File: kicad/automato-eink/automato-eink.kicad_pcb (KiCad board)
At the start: 2 copper layers, 20 parts, among them J1 Conn_01x24, J2 Conn_01x08_Male, Q1 Q_NMOS_GDS

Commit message: first route
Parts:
- added L1: 68uH, Inductor_SMD:L_7.3x7.3_H3.5, F.Cu at (169.0, 107.0)
- moved C11 47.3 mm to (186.3, 95.0)
- moved C3 43.1 mm to (186.2, 108.5)
- moved J1 41.5 mm to (193.8, 107.8), turned to 90 degrees
- moved C12 41.0 mm to (186.3, 92.8)
- moved C6 40.3 mm to (186.2, 101.8)
- moved C9 38.3 mm to (186.3, 110.8)
- moved C4 36.7 mm to (186.2, 106.2)
- moved D1 35.0 mm to (178.0, 101.8)
- moved D3 32.7 mm to (178.0, 107.8), turned to 180 degrees
- moved C5 31.2 mm to (186.3, 104.0)
- moved C10 29.5 mm to (186.3, 97.2)
- moved D2 27.7 mm to (177.9, 104.8), turned to 180 degrees
- moved C7 23.3 mm to (186.2, 113.0)
- moved C8 17.9 mm to (186.2, 99.5)
- moved J2 14.4 mm to (140.2, 117.8), turned to 180 degrees
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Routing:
- net /RST: track 0.00 -> 81.8 mm, vias 0 -> 2
- net /DC: track 0.00 -> 80.8 mm, vias 0 -> 2
- net /CS: track 0.00 -> 80.0 mm, vias 0 -> 2
- net /SCLK: track 0.00 -> 79.0 mm, vias 0 -> 2
- net /BUSY: track 0.00 -> 78.6 mm
- net /SDI: track 0.00 -> 77.9 mm, vias 0 -> 2
- net GND: track 0.00 -> 35.1 mm, vias 0 -> 9
- net /RESE: track 0.00 -> 24.9 mm, vias 0 -> 2
- net /PREVGL: track 0.00 -> 24.5 mm, vias 0 -> 2
- net /PREVGH: track 0.00 -> 22.6 mm, vias 0 -> 2
- net /GDR: track 0.00 -> 18.7 mm, vias 0 -> 2
- net +3V3: track 0.00 -> 15.0 mm, vias 0 -> 2
- net Net-(C12-Pad2): track 0.00 -> 11.6 mm
- net Net-(C10-Pad2): track 0.00 -> 8.26 mm
- net Net-(C2-Pad2): track 0.00 -> 6.69 mm
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- added copper zone on F.Cu, net +3V3
- added copper zone on B.Cu, net GND
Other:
- board outline added: 62.5 x 35 mm
- net class Default: clearance 0.2 -> 0.1524; trace_width 0.25 -> 0.2
- rule trace_clearance: 0.2 -> 0.1524
- board text added: "AUTOMATO EInk rev 1"

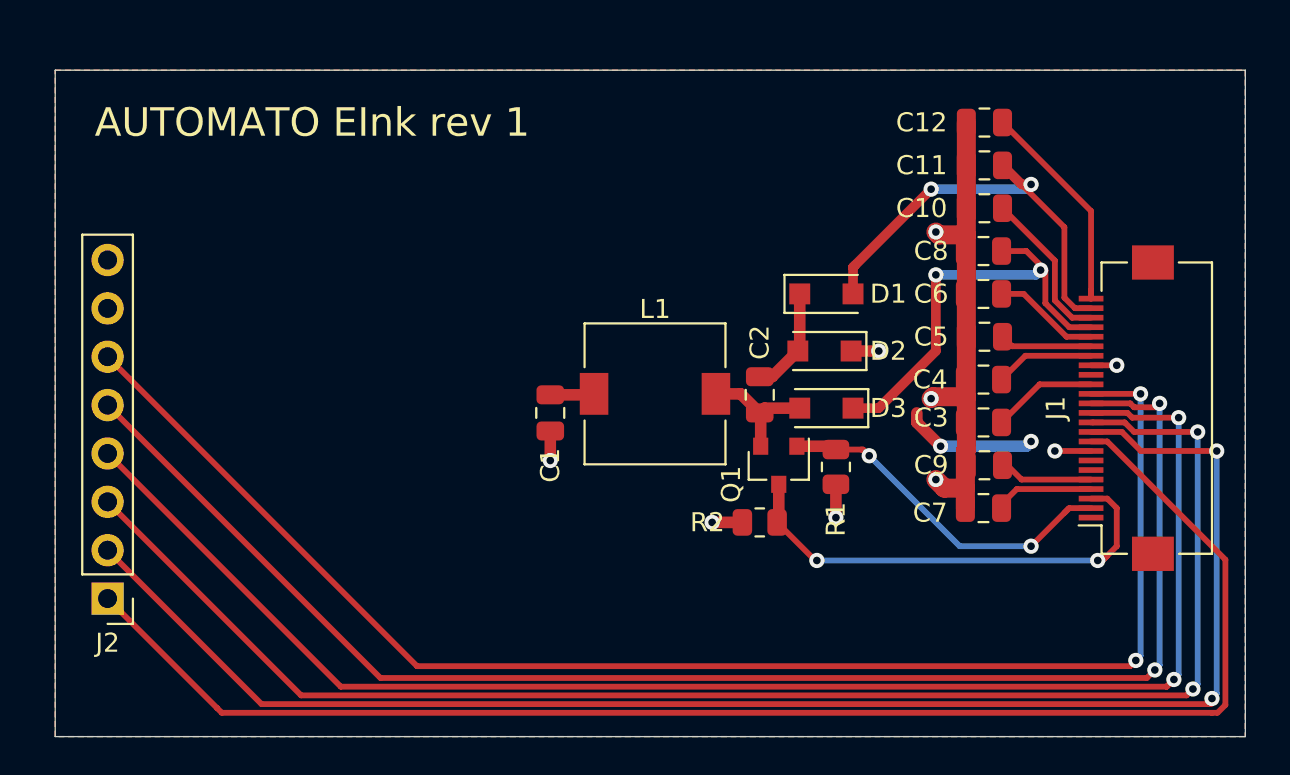
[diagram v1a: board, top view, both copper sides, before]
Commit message: update inductor, add stand-offs
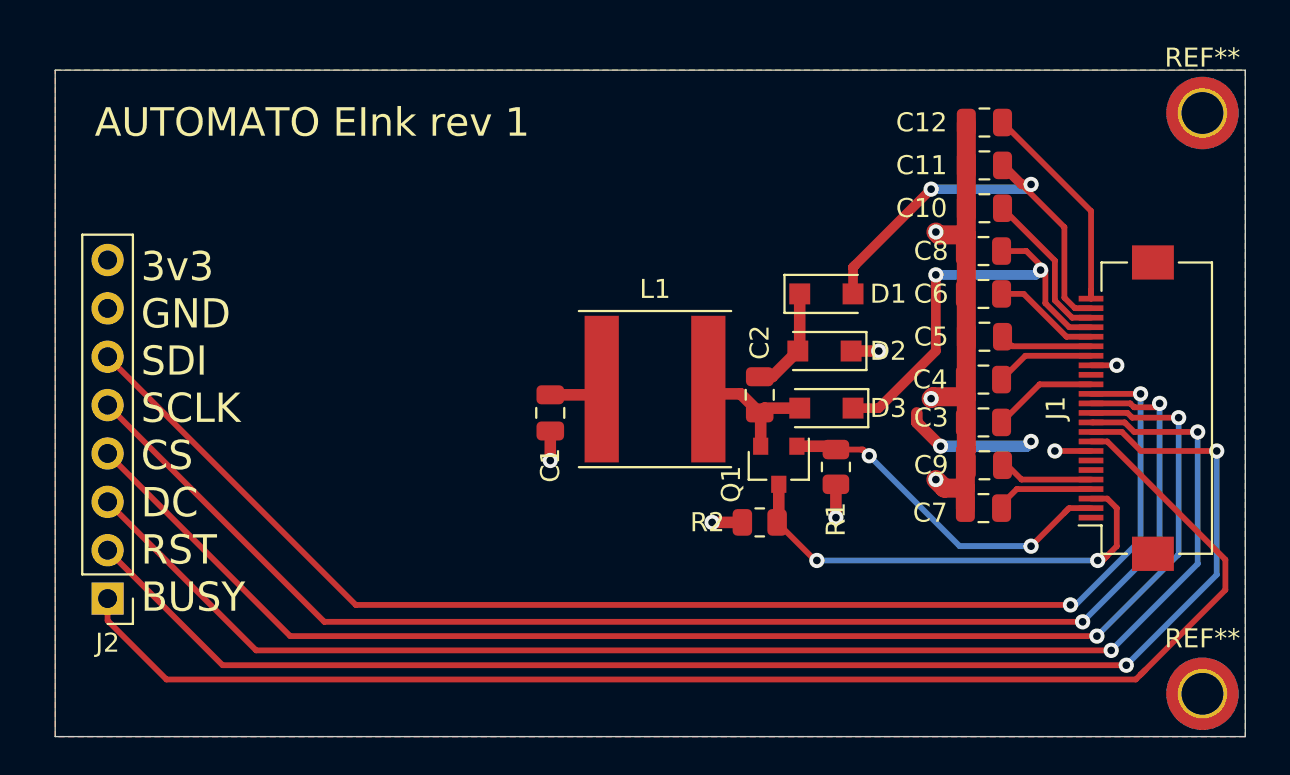
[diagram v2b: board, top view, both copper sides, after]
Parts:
- added REF**: MountingHole_2.2mm_M2_DIN965_Pad_TopBottom, MountingHole:MountingHole_2.2mm_M2_DIN965_Pad_TopBottom, F.Cu at (197.8, 122.8)
- added REF**: MountingHole_2.2mm_M2_DIN965_Pad_TopBottom, MountingHole:MountingHole_2.2mm_M2_DIN965_Pad_TopBottom, F.Cu at (197.8, 92.2)
- L1: footprint Inductor_SMD:L_7.3x7.3_H3.5 -> Inductor_SMD:L_Taiyo-Yuden_NR-80xx
- moved L1 0.25 mm to (169.0, 106.8)
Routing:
- net /SDI: track 77.9 -> 71.6 mm
- net /SCLK: track 79.0 -> 72.8 mm
- net /CS: track 80.0 -> 73.9 mm
- net /DC: track 80.8 -> 75.1 mm
- net /RST: track 81.8 -> 76.2 mm
- net /BUSY: track 78.6 -> 74.7 mm
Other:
- board text added: "3v3 GND SDI SCLK CS DC RST BUSY"
